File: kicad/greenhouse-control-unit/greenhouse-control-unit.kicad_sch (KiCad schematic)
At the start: 45 parts, among them J1 Screw_Terminal_01x02, J10_Buck2 Conn_01x01_Female, J11_Buck2 Conn_01x01_Female, J12_Buck1 Conn_01x01_Female, J13_Buck1 Conn_01x01_Female, J14_Buck2 Conn_01x01_Female, J15_Buck2 Conn_01x01_Female, J16 Screw_Terminal_01x16, J2 Screw_Terminal_01x02, J3 Screw_Terminal_01x02, J4 Screw_Terminal_01x06, J5 Conn_01x03_Male, J6 Conn_01x02_Male, J6_BigBuck1 Conn_01x01_Female, J7_Buck1 Conn_01x01_Female, J8 Conn_01x15_Female, J9 Conn_01x15_Female, Q1 IRLB8721PBF, Q2 IRLB8721PBF, Q3 IRLB8721PBF, Q4 IRLB8721PBF, Q5 IRLB8721PBF, Q6 2N2222A, Q7 2N2222A, Q8 2N2222A, U1 74HC595, U2 74HC595

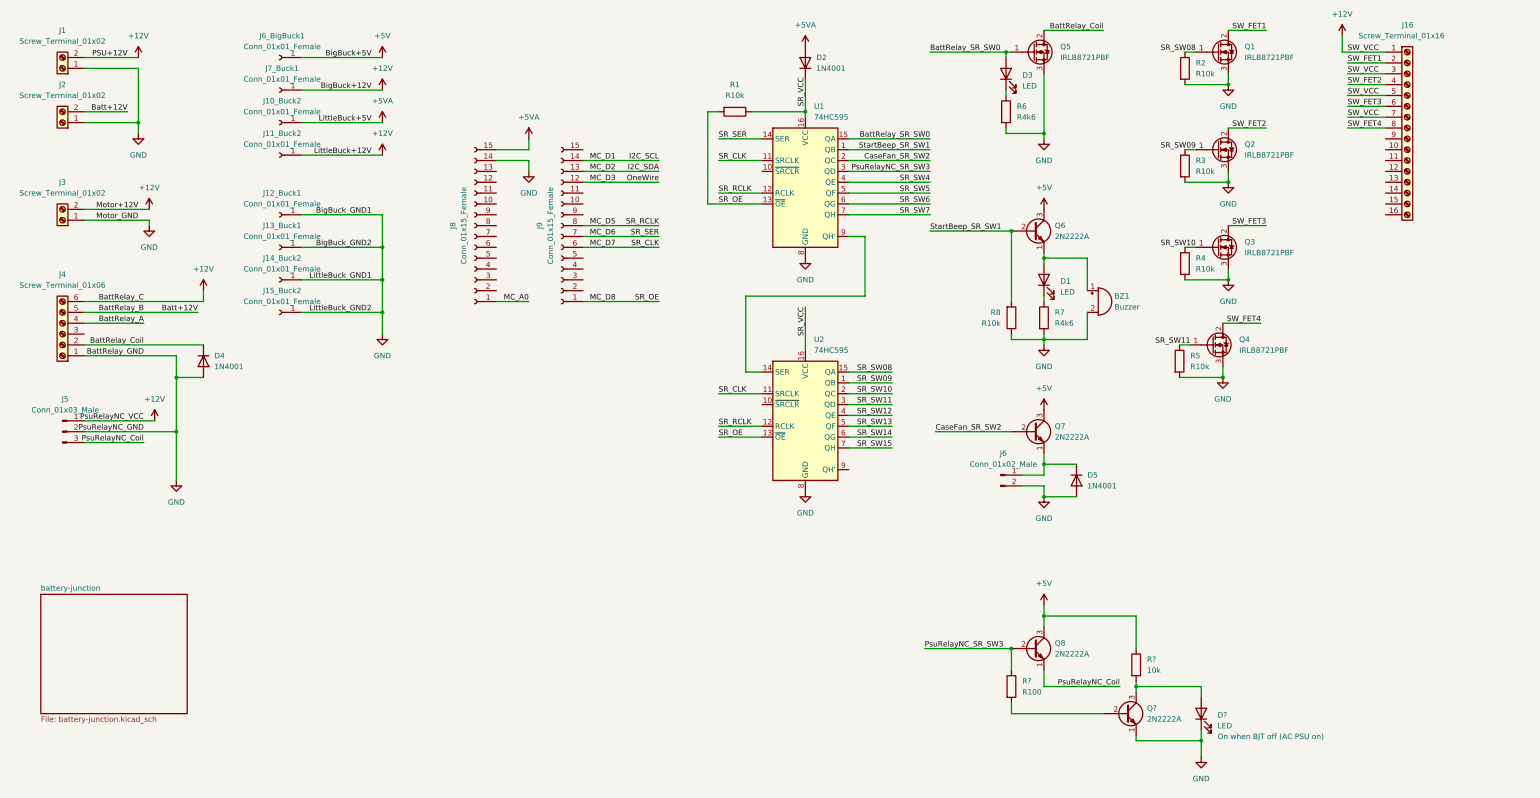
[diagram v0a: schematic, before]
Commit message: Add LED on when FET off
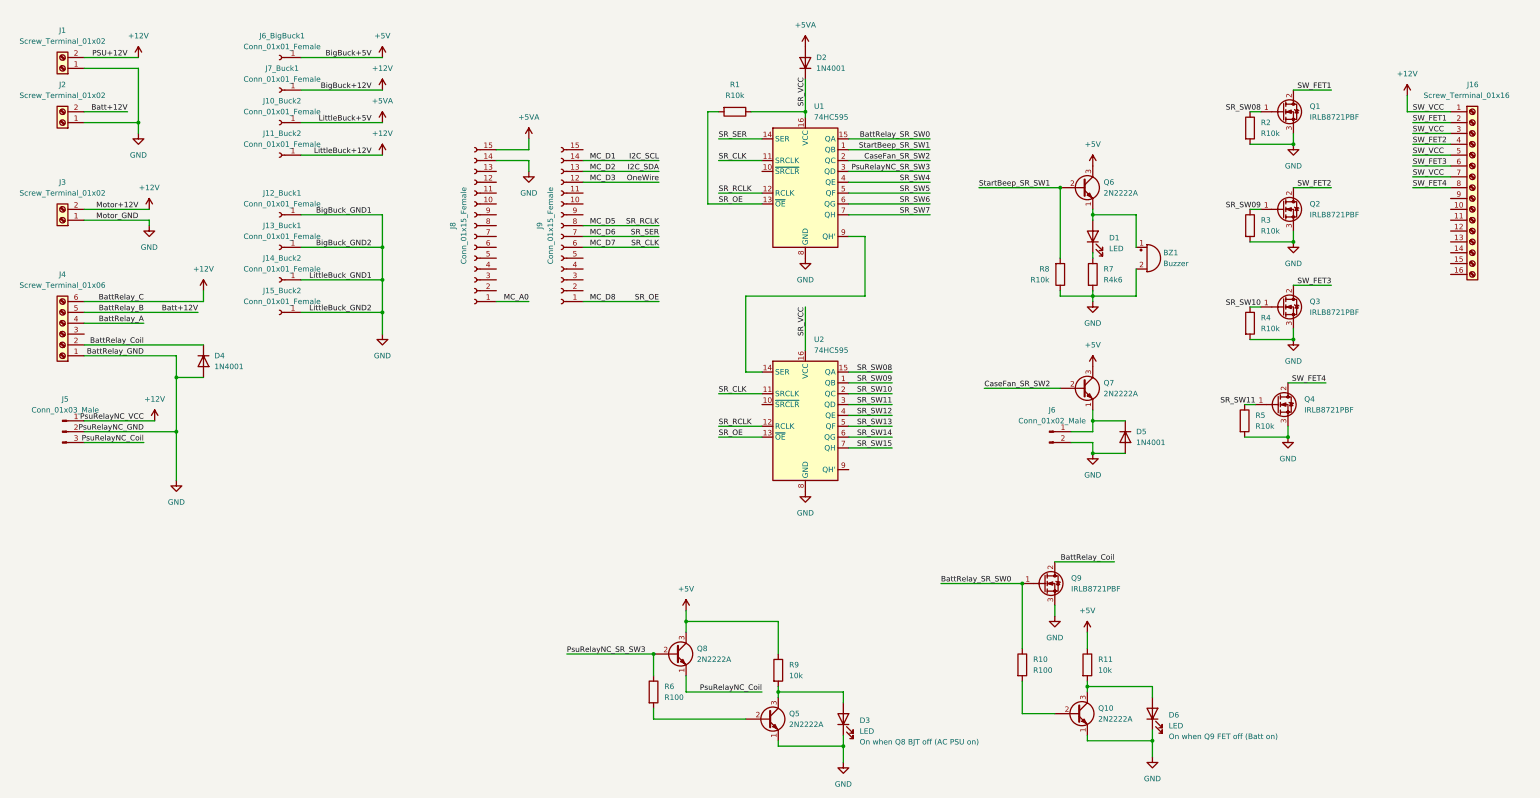
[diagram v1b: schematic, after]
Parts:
- removed D3: LED, LED_THT:LED_D5.0mm, symbol Device:LED
- removed Q5: IRLB8721PBF, Package_TO_SOT_THT:TO-220-3_Vertical, symbol Transistor_FET:IRLB8721PBF
- removed R6: R4k6, Resistor_THT:R_Box_L13.0mm_W4.0mm_P9.00mm, symbol Device:R
- added D6: LED, LED_THT:LED_D5.0mm, symbol Device:LED
- added Q10: 2N2222A, Package_TO_SOT_THT:TO-92_Inline, symbol Nick:2N2222A
- added Q9: IRLB8721PBF, Package_TO_SOT_THT:TO-220-3_Vertical, symbol Transistor_FET:IRLB8721PBF
- added R10: R100, Resistor_THT:R_Box_L8.4mm_W2.5mm_P5.08mm, symbol Device:R
- added R11: 10k, Resistor_THT:R_Box_L8.4mm_W2.5mm_P5.08mm, symbol Device:R
- gave numbers to parts that had none: 4
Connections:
- net +5V: now also R11.1
- net BattRelay_Coil: now also Q9.2 (D)
- net BattRelay_SR_SW0: now also Q9.1 (G), R10.1
- net GND: now also D6.1 (K), Q10.1 (E), Q9.3 (S)
- new net: D6.2 (A), Q10.3 (C), R11.2
- new net: Q10.2 (B), R10.2
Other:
- removed sheet battery-junction
- note added: "On when Q8 BJT off (AC PSU on)"
- note added: "On when Q9 FET off (Batt on)"
- note removed: "On when BJT off (AC PSU on)"
- moved on the sheet: BZ1, D1, D3, D5, J16, J6, Q1, Q2, Q3, Q4, Q5, Q6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

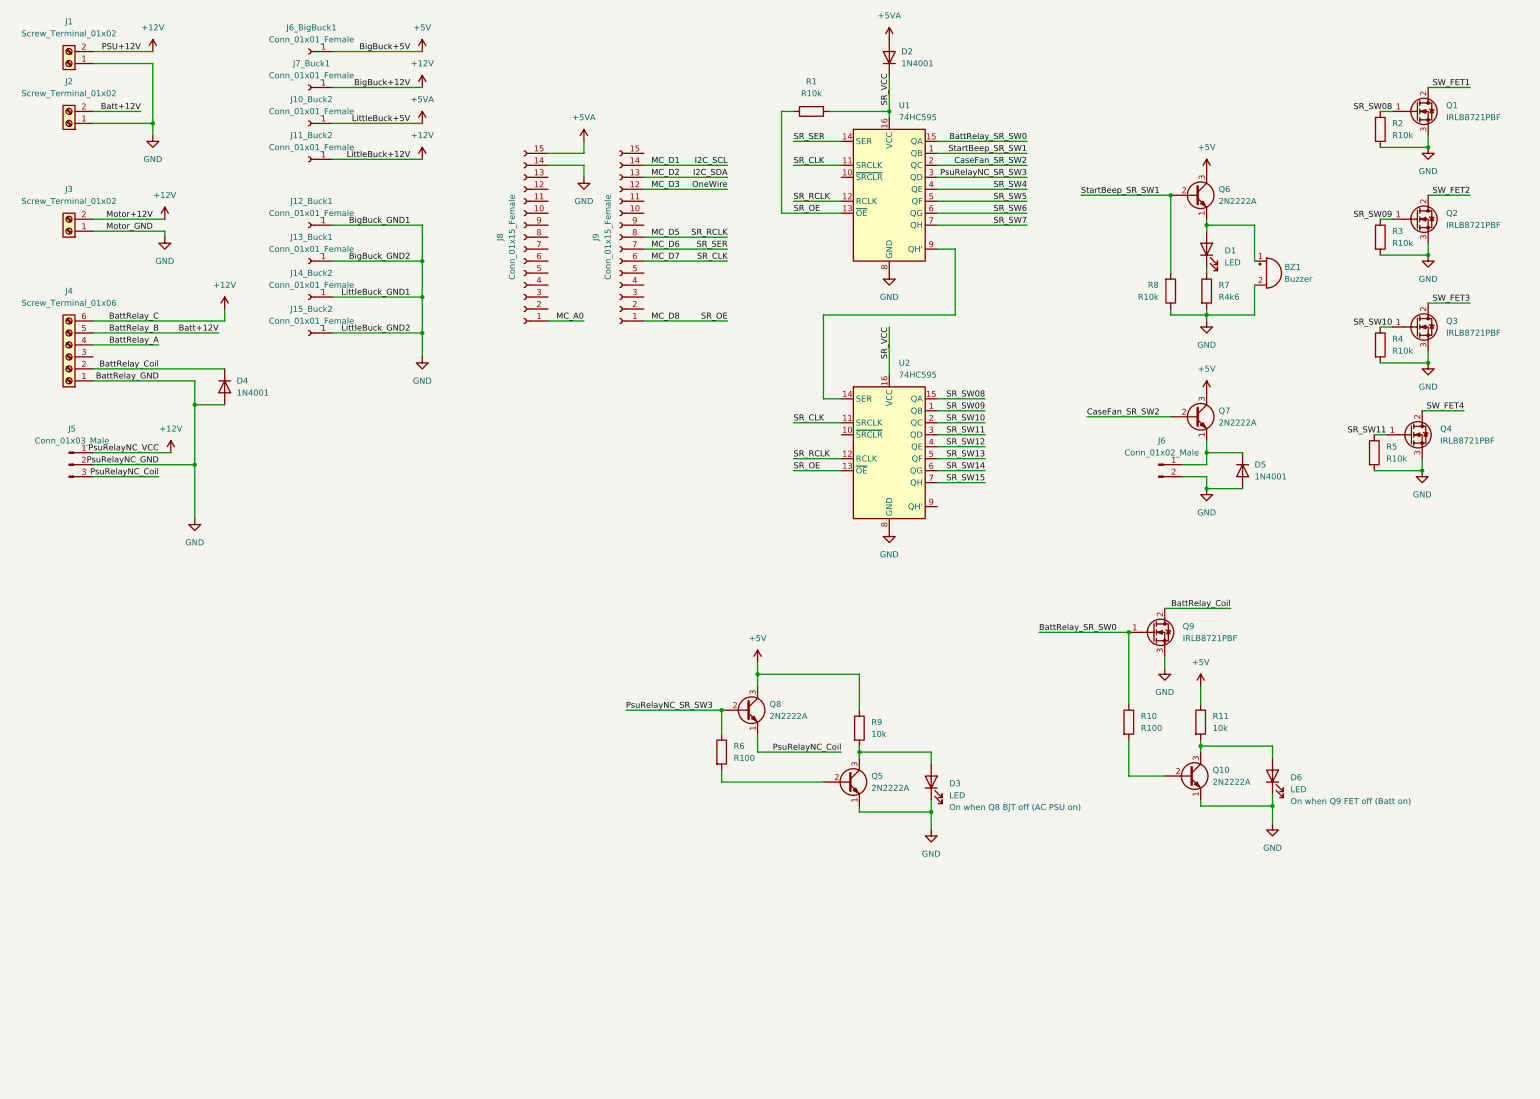
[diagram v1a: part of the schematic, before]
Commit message: Moved power source LEDs to SR, changed label names
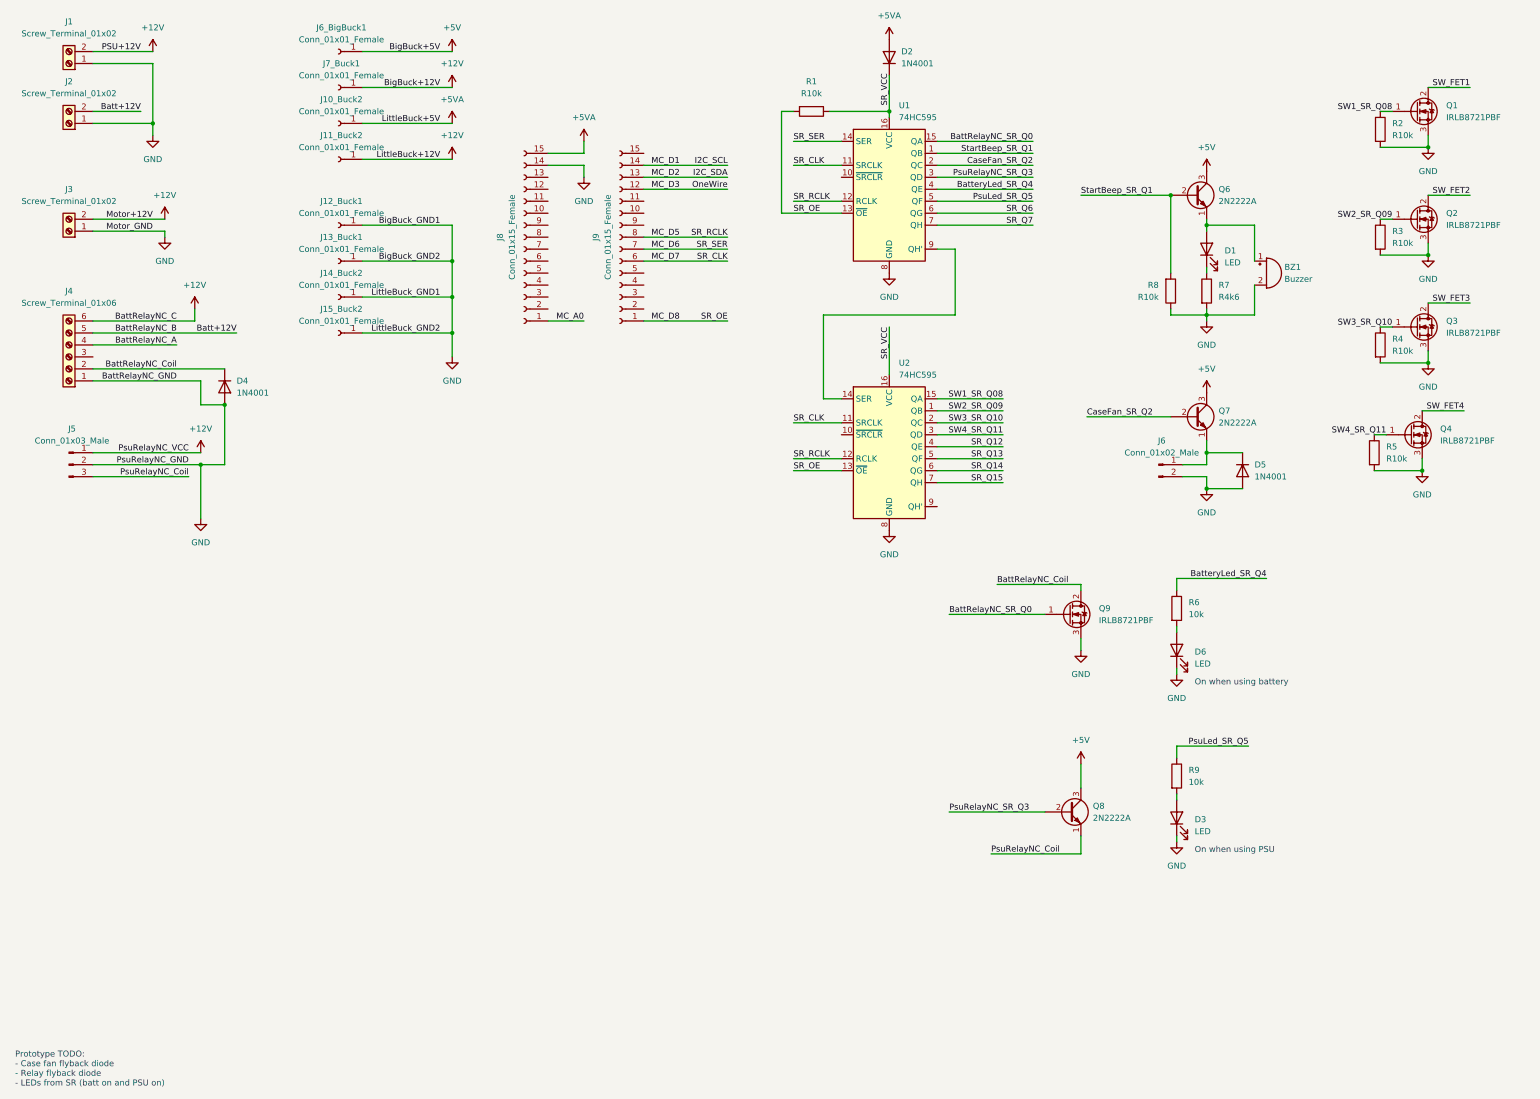
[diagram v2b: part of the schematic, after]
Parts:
- removed Q10, Q5: 2N2222A, Package_TO_SOT_THT:TO-92_Inline, symbol Nick:2N2222A
- removed R10: R100, Resistor_THT:R_Box_L8.4mm_W2.5mm_P5.08mm, symbol Device:R
- removed R11: 10k, Resistor_THT:R_Box_L8.4mm_W2.5mm_P5.08mm, symbol Device:R
- R6: value R100 -> 10k
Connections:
- net +5V: no longer R9.1
- net at D6.2 (A): now also R6.2
- net BattRelay_A renamed BattRelayNC_A
- net BattRelay_Coil renamed BattRelayNC_Coil
- net BattRelay_SR_SW0 renamed BattRelayNC_SR_Q0
- net CaseFan_SR_SW2 renamed CaseFan_SR_Q2
- net PsuRelayNC_SR_SW3 renamed PsuRelayNC_SR_Q3
- net PsuRelayNC_SR_Q3: no longer R6.1
- net SR_SW08 renamed SW1_SR_Q08
- net SR_SW09 renamed SW2_SR_Q09
- net SR_SW10 renamed SW3_SR_Q10
- net SR_SW11 renamed SW4_SR_Q11
- net SR_SW12 renamed SR_Q12
- net SR_SW13 renamed SR_Q13
- net SR_SW14 renamed SR_Q14
- net SR_SW15 renamed SR_Q15
- net SR_SW4 renamed BatteryLed_SR_Q4
- net BatteryLed_SR_Q4: now also R6.1
- net SR_SW5 renamed PsuLed_SR_Q5
- net PsuLed_SR_Q5: now also R9.1
- net SR_SW6 renamed SR_Q6
- net SR_SW7 renamed SR_Q7
- net StartBeep_SR_SW1 renamed StartBeep_SR_Q1
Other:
- note added: "On when using PSU"
- note added: "On when using battery"
- note added: "Prototype TODO: - Case fan flyback diode - Relay flyback diode - LEDs from SR (batt on and PSU on)"
- note removed: "On when Q8 BJT off (AC PSU on)"
- note removed: "On when Q9 FET off (Batt on)"
- moved on the sheet: D3, D6, J10_Buck2, J11_Buck2, J12_Buck1, J13_Buck1, J14_Buck2, J15_Buck2, J6_BigBuck1, J7_Buck1, Q8, Q9
